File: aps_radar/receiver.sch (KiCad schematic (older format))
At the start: 1 part

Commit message: added more
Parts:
- removed U?: hmc951a, symbol aps_radar_lib:hmc951a
- added U?: HMC951A, symbol aps_radar_lib:HMC951A
- added U?: HMC717ALP3E, HCP_16_3, symbol aps_radar_lib:HMC717ALP3E
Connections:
- net labels added: Antenna, IF_I, IF_Q, LOin
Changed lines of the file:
@@
 $EndDescr
 $Comp
-L aps_radar_lib:hmc951a U?
-U 1 1 5E3C6B09
-P 4300 3400
-F 0 "U?" H 4944 3371 50  0000 L CNN
-F 1 "hmc951a" H 4944 3280 50  0000 L CNN
-F 2 "" H 3500 3750 50  0001 C CNN
-F 3 "" H 3500 3750 50  0001 C CNN
-	1    4300 3400
+L aps_radar_lib:HMC951A U?
+U 1 1 5E3DBF7B
+P 7100 3700
+F 0 "U?" H 7100 3211 50  0000 C CNN
+F 1 "HMC951A" H 7100 3120 50  0000 C CNN
+F 2 "" H 6300 4050 50  0001 C CNN
+F 3 "" H 6300 4050 50  0001 C CNN
+	1    7100 3700
 	1    0    0    -1
 $EndComp
+$Comp
+L aps_radar_lib:HMC717ALP3E U?
+U 1 1 5E3DD885
+P 3900 3750
+F 0 "U?" H 4644 3803 60  0000 L CNN
+F 1 "HMC717ALP3E" H 4644 3697 60  0000 L CNN
+F 2 "HCP_16_3" H 3900 4190 60  0001 C CNN
+F 3 "" H 3200 3850 60  0000 C CNN
+	1    3900 3750
+	1    0    0    -1
+$EndComp
+Text HLabel 1100 3900 0    50   Input ~ 0
+Antenna
+Text HLabel 6350 4800 0    50   Input ~ 0
+LOin
+Text HLabel 9350 3300 0    50   Output ~ 0
+IF_I
+Text HLabel 9350 3750 0    50   Output ~ 0
+IF_Q
 $EndSCHEMATC

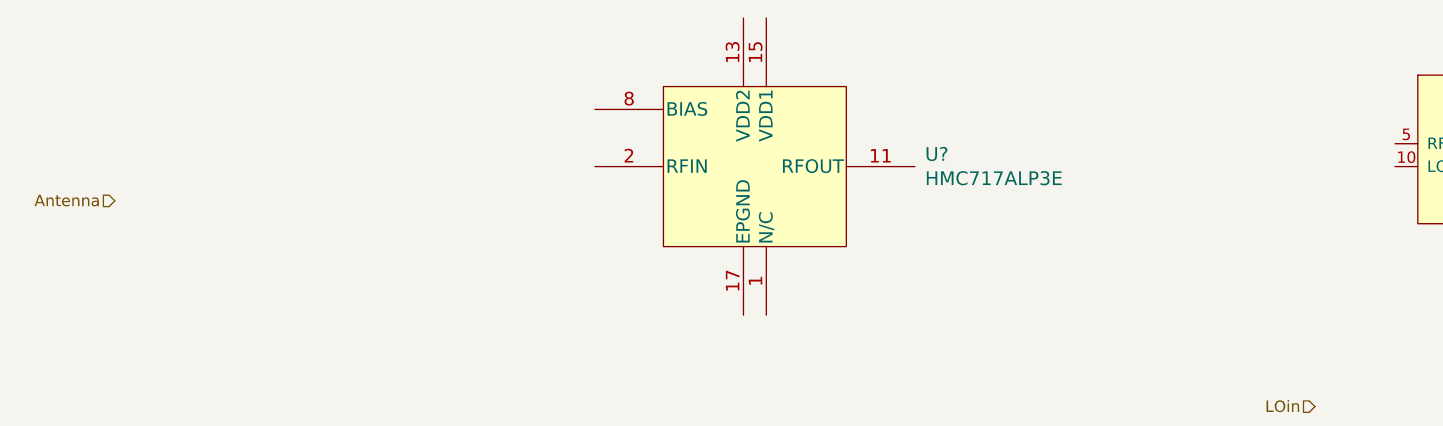
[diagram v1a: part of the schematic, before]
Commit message: Added a capacitor to schem
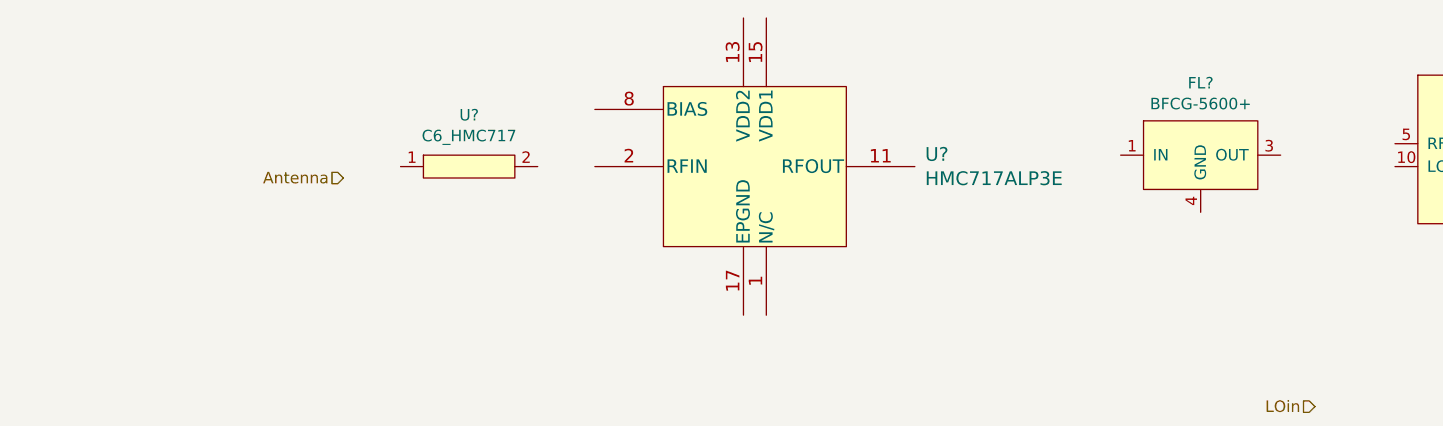
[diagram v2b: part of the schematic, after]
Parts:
- added FL?: BFCG-5600+, apsradar_lib:BFCG_5600+, symbol aps_radar_lib:BFCG-5600+
- added U?: C6_HMC717, symbol aps_radar_lib:C6_HMC717
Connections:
- new net GND: FL?.2 (GND), FL?.4 (GND)
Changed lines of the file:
@@
 	1    0    0    -1
 $EndComp
-Text HLabel 1100 3900 0    50   Input ~ 0
+Text HLabel 2100 3800 0    50   Input ~ 0
 Antenna
 Text HLabel 6350 4800 0    50   Input ~ 0
@@
 Text HLabel 9350 3750 0    50   Output ~ 0
 IF_Q
+$Comp
+L aps_radar_lib:BFCG-5600+ FL?
+U 1 1 5E3DCF63
+P 5850 3700
+F 0 "FL?" H 5850 4015 50  0000 C CNN
+F 1 "BFCG-5600+" H 5850 3924 50  0000 C CNN
+F 2 "apsradar_lib:BFCG_5600+" H 5500 3500 50  0001 C CNN
+F 3 "https://www.minicircuits.com/pdfs/BFCG-5600+.pdf" H 5500 3500 50  0001 C CNN
+	1    5850 3700
+	1    0    0    -1
+$EndComp
+$Comp
+L aps_radar_lib:C6_HMC717 U?
+U 1 1 5E447C0D
+P 2550 3650
+F 0 "U?" H 2650 3775 50  0000 C CNN
+F 1 "C6_HMC717" H 2650 3684 50  0000 C CNN
+F 2 "" H 2550 3650 50  0001 C CNN
+F 3 "" H 2550 3650 50  0001 C CNN
+	1    2550 3650
+	1    0    0    -1
+$EndComp
 $EndSCHEMATC

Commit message: receiver
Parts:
- removed U?: C6_HMC717, symbol aps_radar_lib:C6_HMC717
- added C?: 1.2pF, symbol Device:C_Small
- added C? (x2): 1000 pF, symbol Device:C_Small
- added C? (x4): 100 pF, symbol Device:C_Small
- added C?: 10nF, symbol Device:C_Small
- added C? (x6): 0.01 uF, symbol Device:C_Small
- added C? (x2): 4.7 uF, symbol Device:CP1
- added R? (x2): 0 Ohm, symbol Device:R_Small
- added R?: 825 Ohm, symbol Device:R_Small
- added R? (x6): 500 Ohm, symbol Device:R_Small
- added RV? (x2): 50 KOhm, symbol Device:R_POT_Small
- added U (x2): OPA227, symbol aps_radar_lib:OPA227
- gave numbers to parts that had none: 1
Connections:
- net Antenna: now also C?.2
- net GND: now also U.1 (N/C), U.10 (N/C), U.11 (GND), U.12 (N/C), U.14 (N/C), U.16 (N/C), U.17 (EPGND), U.19 (GND), U.21 (GND), U.22 (GND), U.24 (GND), U.25 (GND), U.3 (N/C), U.4 (GND), U.4 (N/C), U.5 (N/C), U.6 (GND), U.6 (N/C), U.7 (N/C), U.9 (GND), U.9 (N/C), C?.1, C?.1, C?.1, C?.1, C?.1, C?.1, C?.2, C?.2, C?.2, C?.2, C?.2, C?.2, C?.2, R?.2, R?.2, R?.2, U.4 (V-), U.4 (V-)
- net IF_I: now also C?.1, RV?.2, U.6 (Out)
- net IF_Q: now also C?.1, RV?.2, U.6 (Out)
- net LOin: now also U.10 (LOIN)
- net +5V: now reaches U.16 (VDLO)
- net +5V: now also U.2 (VDRF), C?.1, C?.1, C?.1, C?.1, C?.2, C?.2, C?.2, C?.2, C?.2, C?.2, R?.1, R?.1, U.7 (V+), U.7 (V+)
- net at U.20 (IF2): now also R?.2
- net at U.23 (IF1): now also R?.2
- net at U.5 (RFIN): now also FL?.3 (OUT)
- net at FL?.1 (IN): now also U.11 (RFOUT)
- net at U.13 (VDD2): now also R?.2
- net at U.15 (VDD1): now also R?.2
- net at U.2 (RFIN): now also C?.1
- net at U.8 (BIAS): now also C?.1, R?.1
- new net: C?.1, C?.2, R?.1, R?.2 (x2)
- new net: R?.1, U.3 (+In) (x2)
- new net: R?.1, RV?.3, U.2 (-In) (x2)
